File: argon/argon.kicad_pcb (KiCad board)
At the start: 2 copper layers, 60 x 60 mm, 73 parts, among them J1 USB, J2 V3V3-GND, J3 V3V3-GND, J4 V3V3-GND, J5 V3V3-GND, U1 LMC555xM, U2 AMS1117-3.3, U3 93LCxxA, U4 LMC555xM, U5 FT2232HL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

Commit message: 10.16mm between sockets on argon & benzene
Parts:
- moved S1 2.54 mm to (124.5, 131.6)
- moved S2 2.54 mm to (157.5, 131.6)
- moved S3 2.54 mm to (124.5, 129.1)
- moved S4 2.54 mm to (157.5, 129.1)
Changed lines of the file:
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@@
   (general
     (thickness 1.6)
-    (drawings 17)
+    (drawings 18)
     (tracks 0)
     (zones 0)
@@
     (35 F.Paste user hide)
     (36 B.SilkS user)
-    (37 F.SilkS user hide)
+    (37 F.SilkS user)
     (38 B.Mask user hide)
     (39 F.Mask user hide)
@@
   )
   (module Connector_PinHeader_2.54mm:PinHeader_1x08_P2.54mm_Vertical (layer F.Cu)
-    (at 157.48 131.62 90)
+    (at 157.48 129.08 90)
     (descr "Through hole straight pin header, 1x08, 2.54mm pitch, single row")
     (tags "Through hole pin header THT 1x08 2.54mm single row")
@@
   )
   (module Connector_PinHeader_2.54mm:PinHeader_1x08_P2.54mm_Vertical (layer F.Cu)
-    (at 157.48 129.08 90)
+    (at 157.48 131.62 90)
     (descr "Through hole straight pin header, 1x08, 2.54mm pitch, single row")
     (tags "Through hole pin header THT 1x08 2.54mm single row")
@@
   )
   (module Connector_PinHeader_2.54mm:PinHeader_1x08_P2.54mm_Vertical (layer F.Cu)
-    (at 124.46 131.62 90)
+    (at 124.46 129.08 90)
     (descr "Through hole straight pin header, 1x08, 2.54mm pitch, single row")
     (tags "Through hole pin header THT 1x08 2.54mm single row")
@@
   )
   (module Connector_PinHeader_2.54mm:PinHeader_1x08_P2.54mm_Vertical (layer F.Cu)
-    (at 124.46 129.08 90)
+    (at 124.46 131.62 90)
     (descr "Through hole straight pin header, 1x08, 2.54mm pitch, single row")
     (tags "Through hole pin header THT 1x08 2.54mm single row")
@@
     )
   )
+  (dimension 10.16 (width 0.15) (layer Dwgs.User)
+    (gr_text "10.160 mm" (at 183.672 123.952 270) (layer Dwgs.User)
+      (effects (font (size 1 1) (thickness 0.15)))
+    )
+    (feature1 (pts (xy 172.72 129.032) (xy 182.958421 129.032)))
+    (feature2 (pts (xy 172.72 118.872) (xy 182.958421 118.872)))
+    (crossbar (pts (xy 182.372 118.872) (xy 182.372 129.032)))
+    (arrow1a (pts (xy 182.372 129.032) (xy 181.785579 127.905496)))
+    (arrow1b (pts (xy 182.372 129.032) (xy 182.958421 127.905496)))
+    (arrow2a (pts (xy 182.372 118.872) (xy 181.785579 119.998504)))
+    (arrow2b (pts (xy 182.372 118.872) (xy 182.958421 119.998504)))
+  )
   (dimension 20 (width 0.15) (layer Dwgs.User)

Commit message: Argon PCB
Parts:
- moved R16 48.9 mm to (159.5, 123.7)
- moved C23 45.5 mm to (150.4, 121.7), turned to 90 degrees
- moved R10 43.7 mm to (159.5, 125.5), turned to 180 degrees
- moved C19 42.0 mm to (147.8, 103.4), turned to 270 degrees
- moved C21 36.5 mm to (153.2, 103.4), turned to 270 degrees
- moved C22 13.5 mm to (159.8, 113.0), turned to 180 degrees

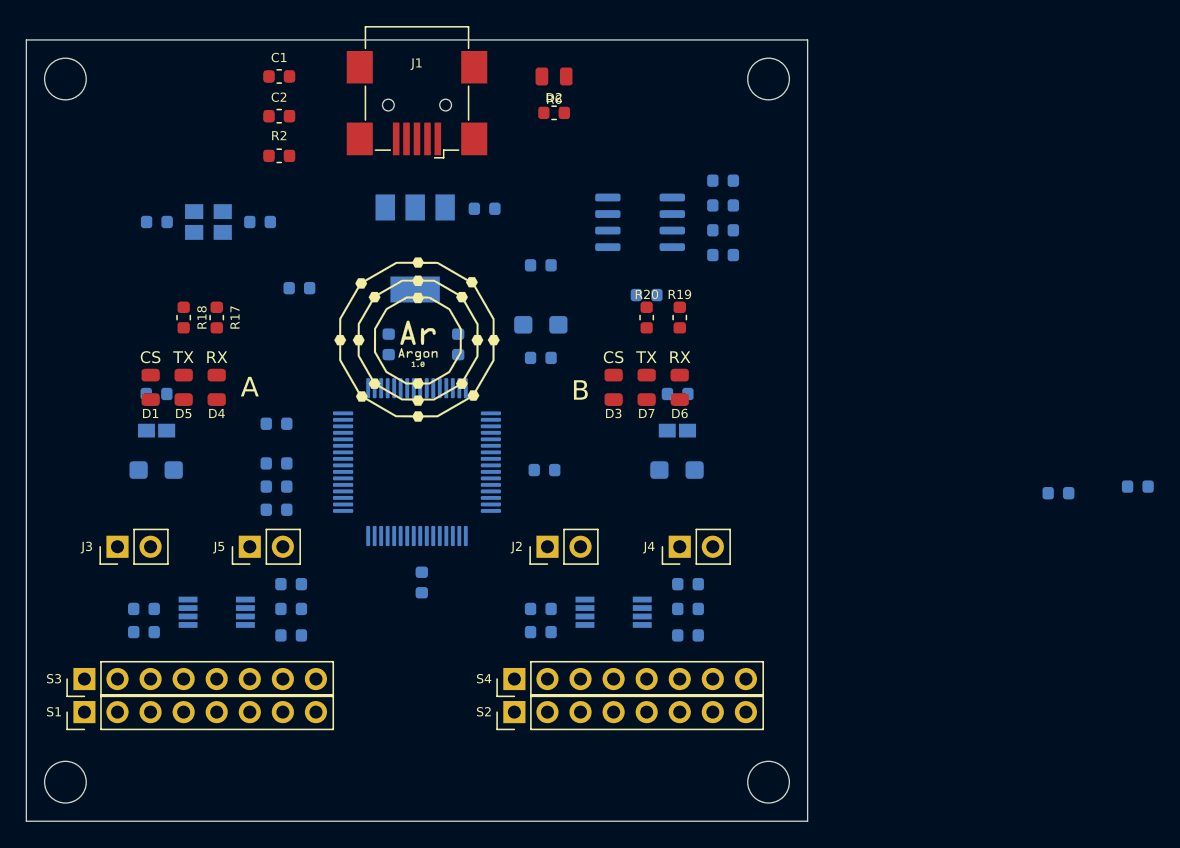
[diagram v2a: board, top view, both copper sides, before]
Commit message: Argon & beznen compatible
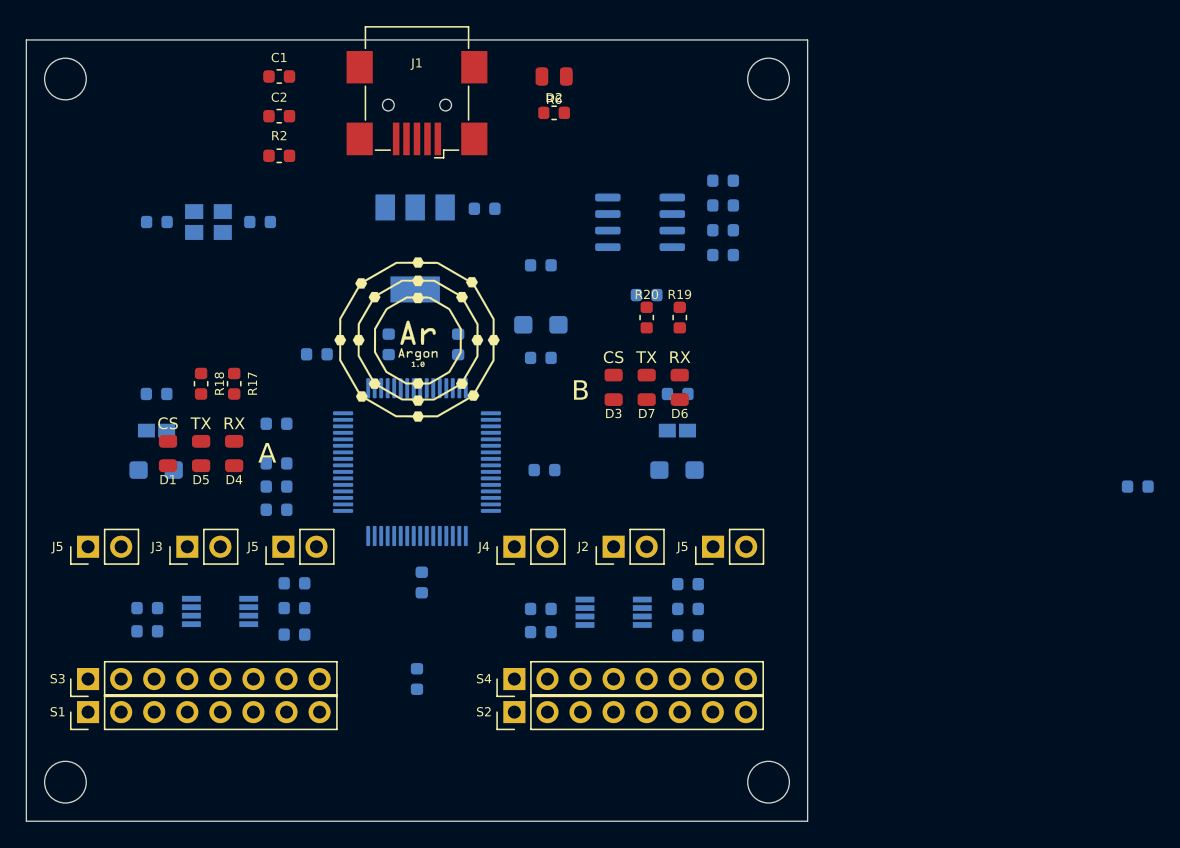
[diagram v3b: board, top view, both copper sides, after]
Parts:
- added J5: V3V3-GND, Connector_PinHeader_2.54mm:PinHeader_1x02_P2.54mm_Vertical, F.Cu at (172.7, 118.9)
- added J5: V3V3-GND, Connector_PinHeader_2.54mm:PinHeader_1x02_P2.54mm_Vertical, F.Cu at (139.7, 118.9)
- moved C20 51.3 mm to (150.0, 129.1), turned to 90 degrees
- moved J4 12.7 mm to (157.5, 118.9)
- moved J5 12.4 mm to (124.7, 118.9)
- moved J3 5.36 mm to (132.4, 118.9)
- moved C5 5.25 mm to (142.3, 104.1)
- moved D1 5.25 mm to (130.9, 111.8)
- moved D4 5.25 mm to (136.0, 111.8)
- moved R17 5.25 mm to (136.0, 106.4)
- moved D5 5.25 mm to (133.4, 111.8)
- moved R18 5.25 mm to (133.4, 106.4)
- moved J2 5.08 mm to (165.1, 118.9)
- moved S1 0.28 mm to (124.7, 131.6)
- moved S3 0.28 mm to (124.7, 129.1)
- moved C3 0.26 mm to (140.6, 121.7)
- moved C6 0.26 mm to (140.6, 125.7)
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
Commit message: Argon - all elements and start paths
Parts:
- removed the J5 at (172.7, 118.9)
- removed the J5 at (139.7, 118.9)
- added C25: 22uF, Capacitor_Tantalum_SMD:CP_EIA-3216-18_Kemet-A, F.Cu at (197.3, 101.8)
- added C5: 22uF, Capacitor_Tantalum_SMD:CP_EIA-3216-18_Kemet-A, F.Cu at (188.0, 109.0)
- added J6: V3V3-GND, Connector_PinHeader_2.54mm:PinHeader_1x02_P2.54mm_Vertical, F.Cu at (165.1, 118.9)
- added J7: V3V3-GND, Connector_PinHeader_2.54mm:PinHeader_1x02_P2.54mm_Vertical, F.Cu at (172.7, 118.9)
- added U6: USBLC6-2SC6, Package_TO_SOT_SMD:SOT-23-6, F.Cu at (150.0, 93.0)
- C3, C9: value 10uF -> 10nF
- moved J2 40.4 mm to (124.7, 118.9)
- moved J5 32.7 mm to (157.5, 118.9)
- moved J4 17.5 mm to (140.0, 118.9)
- moved R6 0.51 mm to (160.5, 86.1)
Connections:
- net Net-(C4-Pad1) renamed VBUS
- R12 pad 2: Net-(J1-Pad2) -> Net-(R12-Pad2)
- R13 pad 2: Net-(J1-Pad3) -> Net-(R13-Pad2)
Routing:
- net Net-(C1-Pad2): track 0.00 -> 31.6 mm
- net Net-(J1-Pad3): track 0.00 -> 9.56 mm
- net VBUS: track 0.00 -> 7.64 mm
- net Net-(J1-Pad2): track 0.00 -> 5.24 mm
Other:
- net class Default: clearance 0.2 -> 0.127; trace_width 0.25 -> 0.127
- net class zasilanie added: clearance 0.381, trace_width 0.381, via_dia 1.143, via_drill 0.508
- rule trace_clearance: 0.2 -> 0.127
- rule trace_min: 0.2 -> 0.1

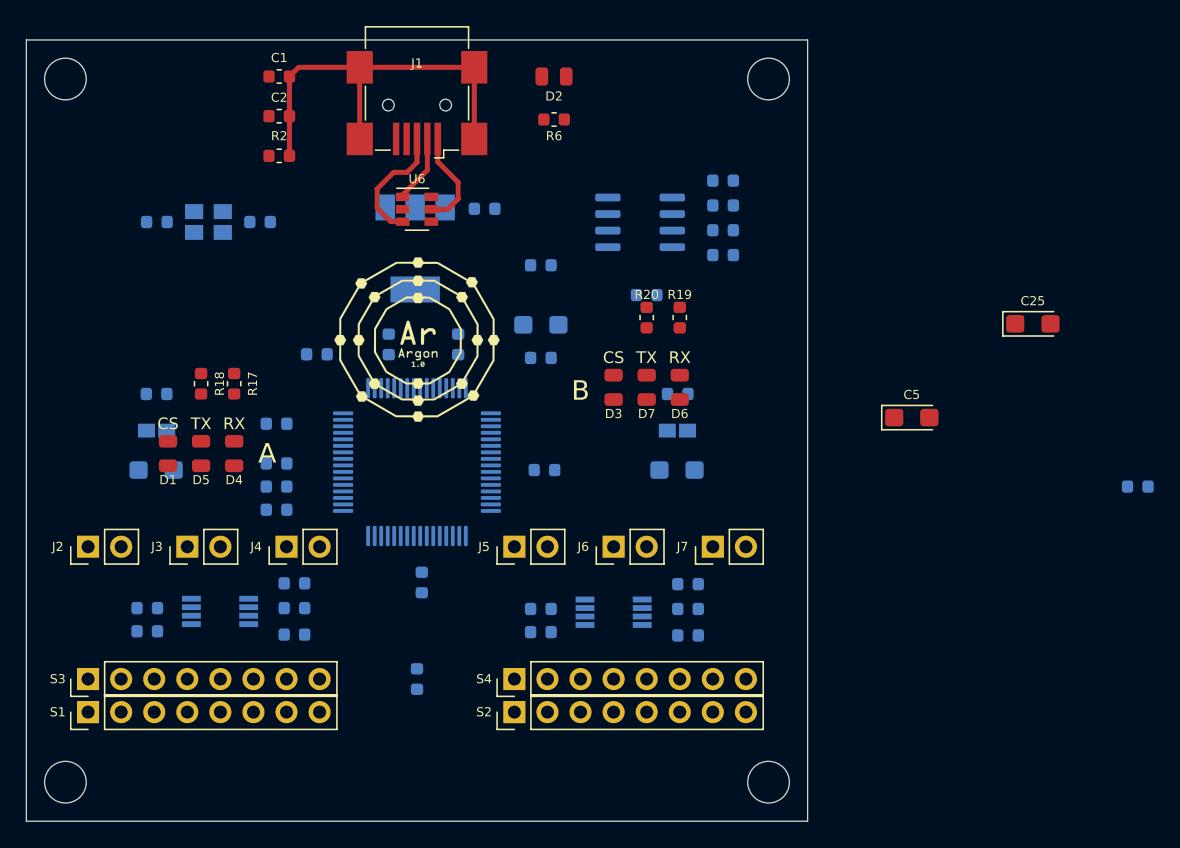
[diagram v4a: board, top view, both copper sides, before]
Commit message: Smaller argon
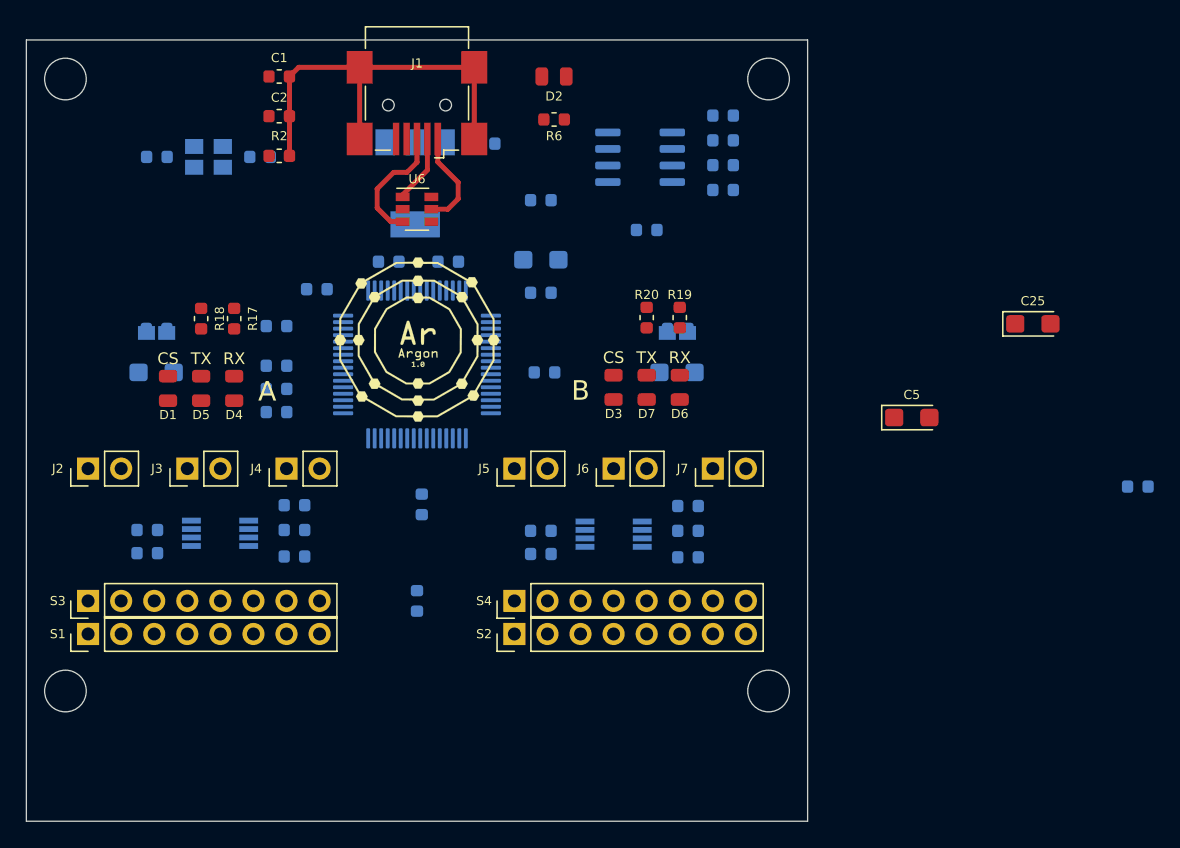
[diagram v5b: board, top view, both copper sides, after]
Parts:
- moved C21 8.29 mm to (147.8, 97.0), turned to 0 degrees
- moved C19 7.82 mm to (152.4, 97.0), turned to 0 degrees
- moved C12 7.50 mm to (170.0, 105.5)
- moved C13 7.50 mm to (130.0, 105.5)
- moved C22 7.50 mm to (159.8, 105.5)
- moved FB1 7.50 mm to (130.0, 102.5)
- moved FB2 7.50 mm to (170.0, 102.5)
- moved R11 7.50 mm to (139.2, 108.6)
- moved R12 7.50 mm to (139.2, 106.8)
- moved R13 7.50 mm to (139.2, 105.0)
- moved R14 7.50 mm to (139.2, 102.0)
- moved U5 7.50 mm to (150.0, 104.9)
- moved H3 7.00 mm to (123.0, 130.0)
- moved H4 7.00 mm to (177.0, 130.0)
- moved C20 6.00 mm to (150.0, 123.1)
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
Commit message: 5x6cm
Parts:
- C4, U2: moved to F.Cu
- moved C25 38.9 mm to (159.3, 93.3)
- moved C5 19.4 mm to (175.8, 94.0), turned to 270 degrees
- moved U2 18.3 mm to (168.0, 89.0), turned to 0 degrees
- moved C4 8.92 mm to (159.3, 95.9), turned to 0 degrees
- moved C24 7.37 mm to (175.0, 95.0)
- moved D4 4.13 mm to (134.9, 102.8)
- moved R17 4.13 mm to (134.9, 97.4)
- moved D1 4.13 mm to (129.9, 102.8)
- moved D5 4.13 mm to (132.4, 102.8)
- moved R18 4.13 mm to (132.4, 97.4)
- moved C12 4.00 mm to (170.0, 101.5)
- moved C13 4.00 mm to (130.0, 101.5)
- moved C14 4.00 mm to (170.0, 98.2)
- moved C15 4.00 mm to (130.0, 98.2)
- moved C17 4.00 mm to (170.8, 115.7)
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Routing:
- net V3V3: track 0.00 -> 111.1 mm
- net VBUS: track 7.64 -> 27.4 mm
- net Net-(D2-Pad2): track 0.00 -> 3.36 mm
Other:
- board size 60 x 60 mm -> 60 x 50 mm

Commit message: PCB wip
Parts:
- moved C16 30.6 mm to (150.0, 119.1), turned to 0 degrees
- moved C8 27.4 mm to (150.0, 121.1)
- moved C7 23.3 mm to (150.0, 114.2), turned to 180 degrees
- moved C14 6.46 mm to (169.9, 104.6)
- moved FB1 3.25 mm to (130.0, 95.2)
- moved C24 2.15 mm to (173.5, 93.5)
- moved C20 1.99 mm to (150.0, 117.1), turned to 0 degrees
- moved C23 0.77 mm to (150.0, 111.0), turned to 180 degrees
- moved C17 0.40 mm to (170.4, 115.7)
- moved C3 0.40 mm to (141.0, 111.7)
- moved C6 0.40 mm to (141.0, 115.7)
- moved C9 0.40 mm to (170.4, 111.8)
- moved J2 0.40 mm to (125.1, 108.9)
- moved J4 0.40 mm to (140.4, 108.9)
- moved J6 0.40 mm to (164.7, 108.9)
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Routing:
- net V3V3: track 111.1 -> 163.5 mm, vias 0 -> 1
- net Net-(C11-Pad1): track 0.00 -> 28.3 mm, vias 0 -> 2
- net Net-(C10-Pad1): track 0.00 -> 27.1 mm
- net Net-(D3-Pad2): track 0.00 -> 9.72 mm
- net Net-(R11-Pad2): track 0.00 -> 5.32 mm
- net Net-(R12-Pad1): track 0.00 -> 4.79 mm
- net Net-(R14-Pad2): track 0.00 -> 4.41 mm
- net Net-(R13-Pad1): track 0.00 -> 4.39 mm
- net Net-(D7-Pad2): track 0.00 -> 3.63 mm
- net Net-(D6-Pad2): track 0.00 -> 3.63 mm
- net Net-(D5-Pad2): track 0.00 -> 3.63 mm
- net Net-(D4-Pad2): track 0.00 -> 3.63 mm
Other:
- board text added: "3V3"
- board text added: "CTS"
- board text added: "DCD"
- board text added: "DSR"
- board text added: "DTR"
- board text added: "GND"
- board text added: "RI"
- board text added: "RTS"
